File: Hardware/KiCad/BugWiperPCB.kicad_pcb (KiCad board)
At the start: 2 copper layers, 112 x 40 mm, 95 parts, among them J1 UJ20-C-H-G-SMT-1-P16-TR, J2 TBLH10-350-06BK, J3 Phoenix_1776508, J4 RJ45, Q1 NMOS_SO-8, U1 ESP32-S3-WROOM-1, U2 BTN9960LV, U3 BTN9960LV, U4 INA180A2, U5 WE-TVS-82400102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

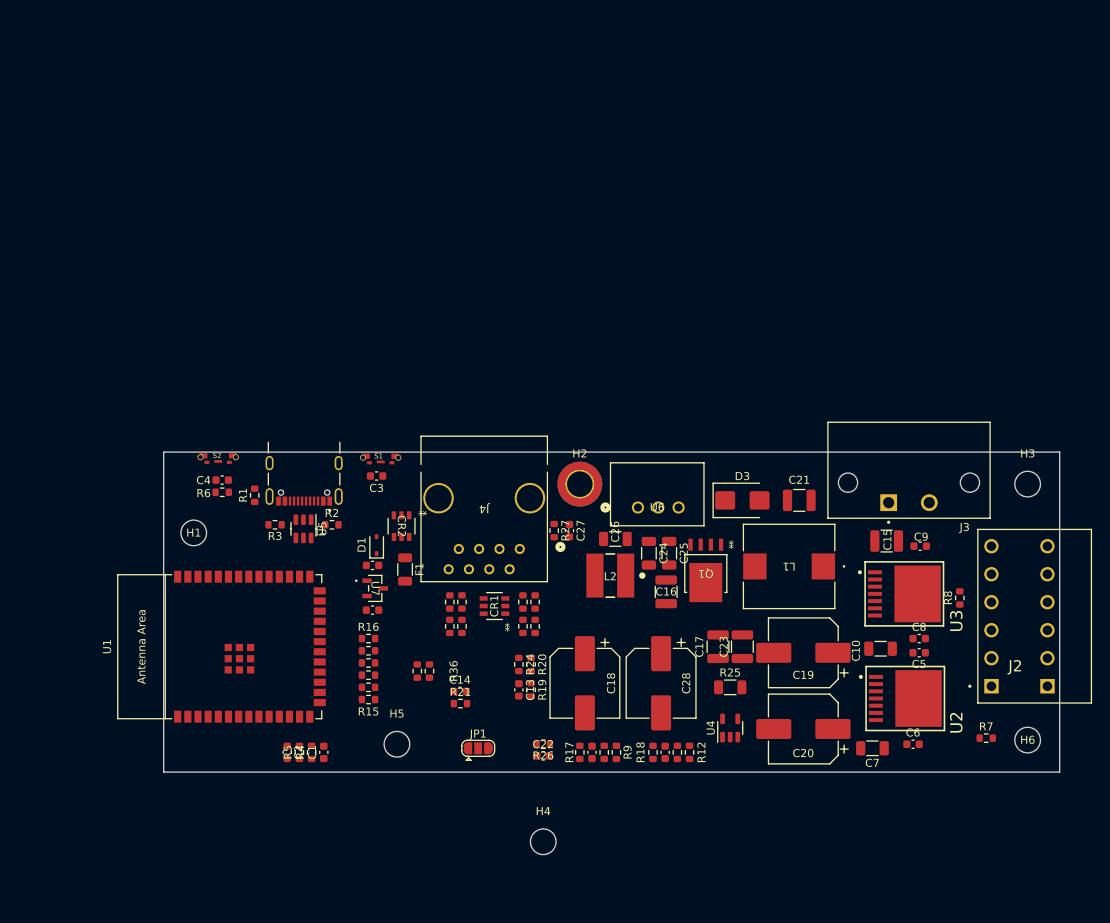
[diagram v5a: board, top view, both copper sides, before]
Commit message: add debug connector, arrange foodprints and add NTC and connect to GPIOs to ESP32
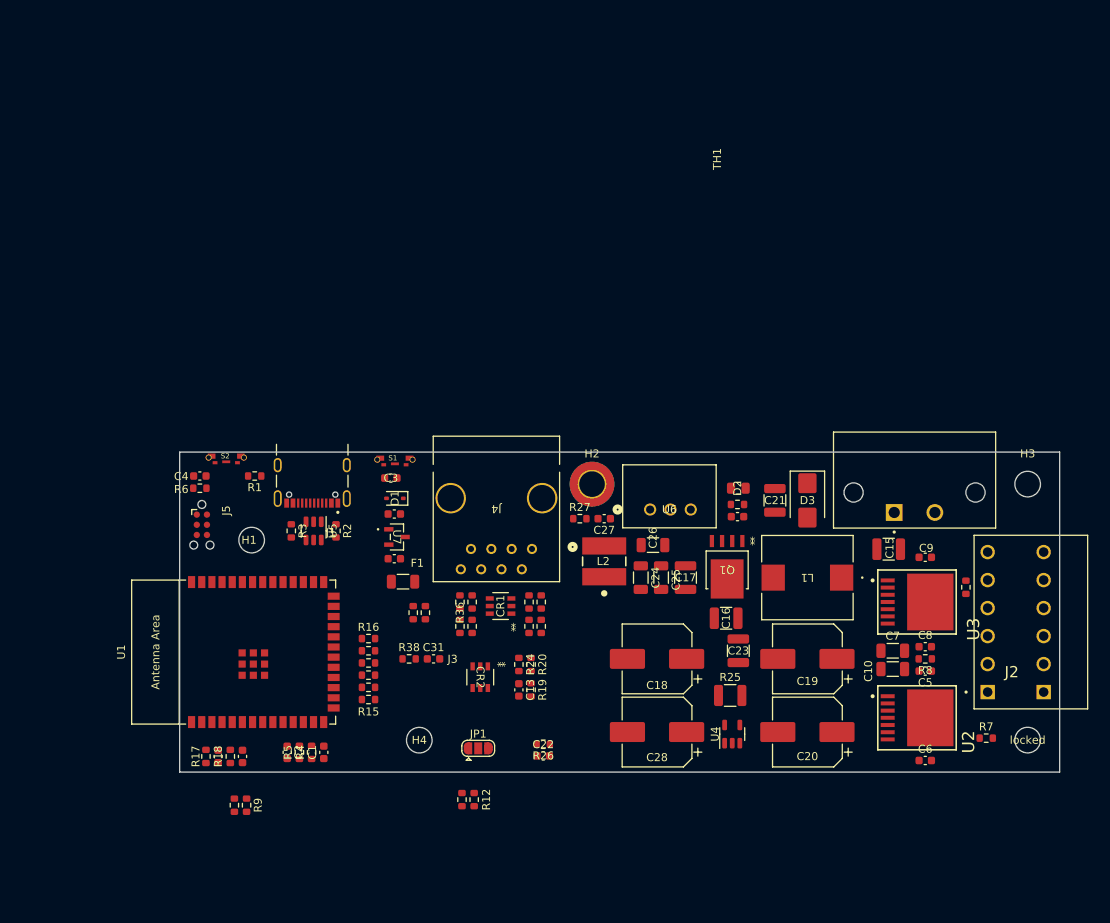
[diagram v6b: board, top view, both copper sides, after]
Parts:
- removed H5: MountingHole, MountingHole:MountingHole_3.2mm_M3_DIN965
- added C31: 100nF, Capacitor_SMD:C_0603_1608Metric, F.Cu at (141.7, 85.9)
- added D2: D_Zener, Resistor_SMD:R_0805_2012Metric, F.Cu at (179.8, 64.5)
- added J5: Conn_TagConnect_TC2030-NL_ESP_Prog, Connector:Tag-Connect_TC2030-IDC-NL_2x03_P1.27mm_Vertical, F.Cu at (112.8, 69.1)
- added R38: 10k, Resistor_SMD:R_0603_1608Metric, F.Cu at (138.7, 85.9)
- added TH1: Thermistor_NTC, Resistor_SMD:R_0603_1608Metric, F.Cu at (208.3, 76.9)
- C4: value 100nF -> 1uF
- R12, R9: value 2k -> 1k
- R25: footprint Resistor_SMD:R_1206_3216Metric -> Resistor_SMD:R_1210_3225Metric
- moved C12 52.8 mm to (117.9, 98.0)
- moved R18 52.8 mm to (116.3, 98.0)
- moved C11 46.7 mm to (114.8, 98.0)
- moved R17 46.7 mm to (113.3, 98.0)
- moved R10 46.7 mm to (116.8, 104.1)
- moved R9 46.7 mm to (118.4, 104.1)
- moved R21 42.6 mm to (179.7, 66.5)
- moved C14 41.0 mm to (179.7, 68.1)
- moved R11 27.6 mm to (145.3, 103.4)
- moved R12 27.6 mm to (146.8, 103.4)
- moved CR2 21.3 mm to (147.6, 88.1)
- moved H4 20.0 mm to (140.0, 96.0)
- moved C7 12.5 mm to (199.1, 84.8), turned to 0 degrees
- moved C17 9.54 mm to (173.2, 75.7)
- moved C18 9.52 mm to (169.7, 85.9), turned to 180 degrees
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- renumbered H6 to locked
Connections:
- net CHIP_PU renamed EN
- net GPIO0 renamed Boot
- C1 pad 2: D+ -> Net-(C1-Pad2)
- C2 pad 1: D- -> Net-(C2-Pad1)
- C22 pad 1: /Power/adc_ina -> /ESP32-S3/ADC_INA
- R17 pad 1: /Power/M_IS1 -> /ESP32-S3/M_IS1
- R18 pad 1: /Power/M_IS2 -> /ESP32-S3/M_IS2
- R24 pad 1: unconnected-(R24-Pad1) -> Net-(U1-GPIO4/TOUCH4/ADC1_CH3)
- R26 pad 2: /Power/adc_ina -> /ESP32-S3/ADC_INA
- R32 pad 1: IN_3 -> IN_4
- R34 pad 1: IN_4 -> IN_3
- R4 pad 1: Net-(U1-GPIO20/U1CTS/ADC2_CH9/CLK_OUT1/USB_D+) -> Net-(C1-Pad2)
- R5 pad 1: Net-(U1-GPIO19/U1RTS/ADC2_CH8/CLK_OUT2/USB_D-) -> Net-(C2-Pad1)
- U1 pad 12: unconnected-(U1-GPIO8/TOUCH8/ADC1_CH7/SUBSPICS1-Pad12) -> OUT1
- U1 pad 13: Net-(U1-GPIO19/U1RTS/ADC2_CH8/CLK_OUT2/USB_D-) -> D-
- U1 pad 14: Net-(U1-GPIO20/U1CTS/ADC2_CH9/CLK_OUT1/USB_D+) -> D+
- U1 pad 17: unconnected-(U1-GPIO9/TOUCH9/ADC1_CH8/FSPIHD/SUBSPIHD-Pad17) -> OUT2
- U1 pad 20: unconnected-(U1-GPIO12/TOUCH12/ADC2_CH1/FSPICLK/FSPIIO6/SUBSPICLK-Pad20) -> IN_1
- U1 pad 21: unconnected-(U1-GPIO13/TOUCH13/ADC2_CH2/FSPIQ/FSPIIO7/SUBSPIQ-Pad21) -> IN_2
- U1 pad 22: unconnected-(U1-GPIO14/TOUCH14/ADC2_CH3/FSPIWP/FSPIDQS/SUBSPIWP-Pad22) -> IN_3
- U1 pad 23: unconnected-(U1-GPIO21-Pad23) -> IN_4
- U1 pad 36: unconnected-(U1-U0RXD/GPIO44/CLK_OUT2-Pad36) -> RX
- U1 pad 37: unconnected-(U1-U0TXD/GPIO43/CLK_OUT1-Pad37) -> TX
- U1 pad 39: unconnected-(U1-GPIO1/TOUCH1/ADC1_CH0-Pad39) -> /ESP32-S3/ADC_NTC
- U1 pad 4: unconnected-(U1-GPIO4/TOUCH4/ADC1_CH3-Pad4) -> Net-(U1-GPIO4/TOUCH4/ADC1_CH3)
- U1 pad 5: unconnected-(U1-GPIO5/TOUCH5/ADC1_CH4-Pad5) -> /ESP32-S3/M_IS1
- U1 pad 6: unconnected-(U1-GPIO6/TOUCH6/ADC1_CH5-Pad6) -> /ESP32-S3/M_IS2
- U1 pad 7: unconnected-(U1-GPIO7/TOUCH7/ADC1_CH6-Pad7) -> /ESP32-S3/ADC_INA
- U5 pad 4: D+ -> Net-(C1-Pad2)
- U5 pad 6: D- -> Net-(C2-Pad1)
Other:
- board size 112 x 40 mm -> 110 x 40 mm

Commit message: add resistor arrays
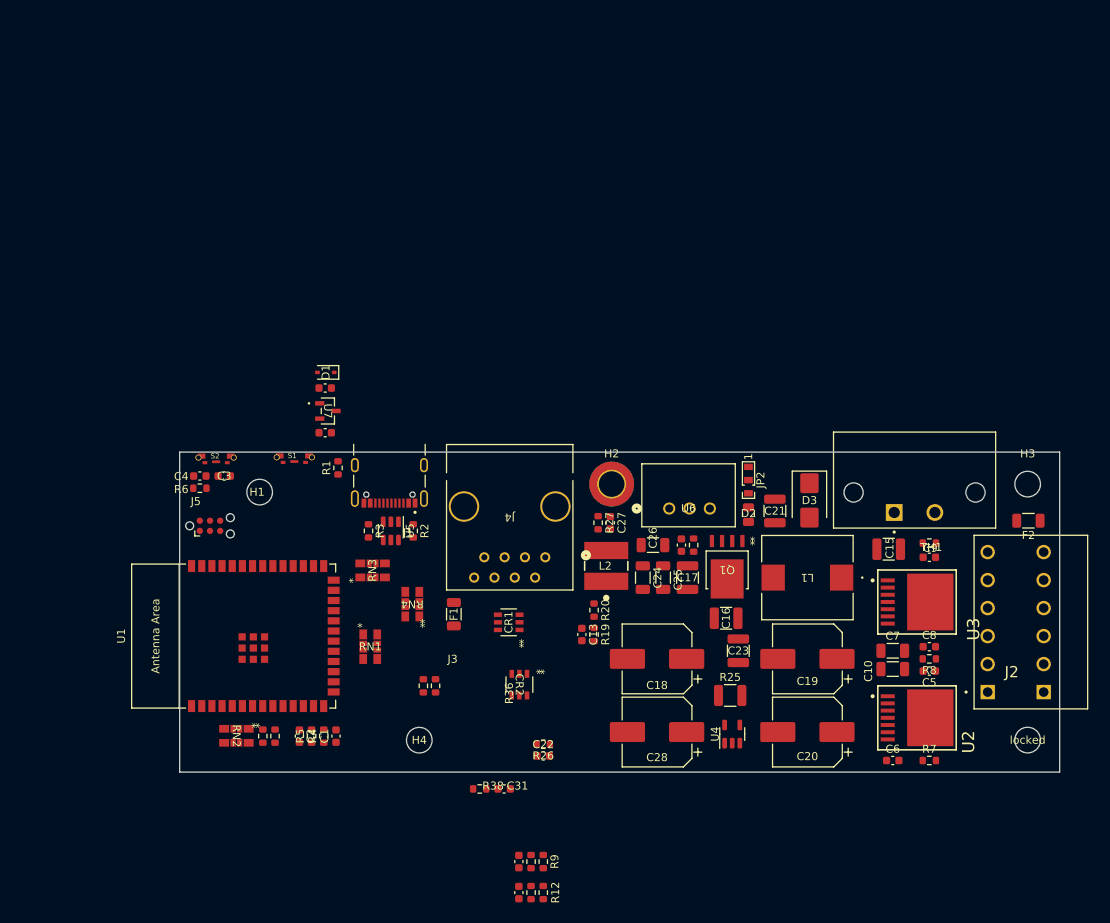
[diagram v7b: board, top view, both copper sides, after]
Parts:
- removed JP1: SolderJumper_3_Bridged12, Jumper:SolderJumper-3_P1.3mm_Open_RoundedPad1.0x1.5mm
- removed R13, R14, R15, R16, R17, R18, R24, R29, R34: 1k, Resistor_SMD:R_0603_1608Metric
- removed R28, R32: 4k7, Resistor_SMD:R_0603_1608Metric
- removed R30, R31, R33, R35: 5k, Resistor_SMD:R_0603_1608Metric
- added F2: 10mA Polyfuse, Resistor_SMD:R_1206_3216Metric, F.Cu at (216.1, 68.6)
- added JP2: SolderJumper_3_Open, BugWiper_lib:SolderJumper_R_SMD_0603, F.Cu at (181.1, 63.5)
- added RN1: 1k_Pack04, BugWiper_lib:BO_CAY16, F.Cu at (133.8, 84.3)
- added RN2: 1k_Pack04, BugWiper_lib:BO_CAY16, F.Cu at (117.1, 95.5)
- added RN3: 10k_Pack04, BugWiper_lib:BO_CAY16, F.Cu at (134.1, 74.8)
- added RN4: 10k_Pack04, BugWiper_lib:BO_CAY16, F.Cu at (139.1, 79.0)
- moved C11 39.8 mm to (152.4, 111.2)
- moved C12 38.5 mm to (152.4, 115.1)
- moved R10 37.7 mm to (153.9, 111.2)
- moved R9 37.7 mm to (155.4, 111.2)
- moved C3 20.8 mm to (115.6, 63.0), turned to 180 degrees
- moved C31 18.5 mm to (150.6, 102.1)
- moved R38 18.5 mm to (147.5, 102.1)
- moved C29 18.0 mm to (128.2, 57.6)
- moved D1 18.0 mm to (128.3, 50.0)
- moved C30 18.0 mm to (128.2, 52.0)
- moved U7 18.0 mm to (128.5, 54.9)
- moved R22 17.0 mm to (120.4, 95.5), turned to -90 degrees
- moved R23 14.8 mm to (121.9, 95.5), turned to -90 degrees
- moved R11 14.5 mm to (153.9, 115.1)
- moved R12 14.5 mm to (155.4, 115.1)
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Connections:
- net +3V3 renamed Net-(J2-3)
- C11 pad 1: Net-(C11-Pad1) -> /ESP32-S3/M_IS1
- C12 pad 1: Net-(C12-Pad1) -> /ESP32-S3/M_IS2
- J4 pad 2: Net-(CR1-IO_2) -> Net-(CR1-IO_1)
- J4 pad 3: Net-(CR1-IO_1) -> Net-(CR1-IO_2)
- J4 pad 6: Net-(CR1-IO_4) -> Net-(CR1-IO_3)
- J4 pad 7: Net-(CR1-IO_3) -> Net-(CR1-IO_4)
- R10 pad 1: Net-(C11-Pad1) -> /ESP32-S3/M_IS1
- R11 pad 1: Net-(C12-Pad1) -> /ESP32-S3/M_IS2
- U1 pad 18: unconnected-(U1-GPIO10/TOUCH10/ADC1_CH9/FSPICS0/FSPIIO4/SUBSPICS0-Pad18) -> M__IN1
- U1 pad 19: unconnected-(U1-GPIO11/TOUCH11/ADC2_CH0/FSPID/FSPIIO5/SUBSPID-Pad19) -> M__IN2
- U1 pad 20: IN_1 -> M__INH1
- U1 pad 21: IN_2 -> M__INH2
- U1 pad 22: IN_3 -> IN_1
- U1 pad 23: IN_4 -> IN_2
- U1 pad 24: unconnected-(U1-GPIO47/SPICLK_P/SUBSPICLK_P_DIFF-Pad24) -> IN_3
- U1 pad 25: unconnected-(U1-GPIO48/SPICLK_N/SUBSPICLK_N_DIFF-Pad25) -> IN_4
- U1 pad 39: /ESP32-S3/ADC_NTC -> A_INA
- U1 pad 4: Net-(U1-GPIO4/TOUCH4/ADC1_CH3) -> A_VBAT
- U1 pad 5: /ESP32-S3/M_IS1 -> A_NTC
- U1 pad 6: /ESP32-S3/M_IS2 -> A_IS2
- U1 pad 7: /ESP32-S3/ADC_INA -> A_IS1
- U1 pad 8: unconnected-(U1-GPIO15/U0RTS/ADC2_CH4/XTAL_32K_P-Pad8) -> Enc1
- U1 pad 9: unconnected-(U1-GPIO16/U0CTS/ADC2_CH5/XTAL_32K_N-Pad9) -> Enc2
- U2 pad 3: Net-(U2-IN) -> /ESP32-S3/M_IN1
- U2 pad 4: Net-(U2-INH) -> /ESP32-S3/M_INH1
- U3 pad 3: Net-(U3-IN) -> /ESP32-S3/M_IN2
- U3 pad 4: Net-(U3-INH) -> /ESP32-S3/M_IHN2

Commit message: begin routing
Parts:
- removed R22, R23, R26: 1k, Resistor_SMD:R_0603_1608Metric
- removed R36, R37: 330, Resistor_SMD:R_0603_1608Metric
- added R13: 1k, Resistor_SMD:R_0603_1608Metric, F.Cu at (149.3, 92.5)
- added RN5: 1k_Pack04, BugWiper_lib:BO_CAY16, F.Cu at (121.9, 95.0)
- added RN6: 100R_Pack04, BugWiper_lib:BO_CAY16, F.Cu at (148.8, 80.8)
- added RN7: 100R_Pack04, BugWiper_lib:BO_CAY16, F.Cu at (154.4, 80.8)
- D1: footprint Diode_SMD:D_SOD-323 -> Diode_SMD:D_SOD-323_HandSoldering
- RN3: value 10k_Pack04 -> 47k_Pack04
- RN4: value 10k_Pack04 -> 2k2_Pack04
- moved C2 28.3 mm to (138.9, 70.9), turned to 90 degrees
- moved C1 25.0 mm to (133.9, 70.9), turned to -90 degrees
- moved C11 20.8 mm to (154.4, 90.5)
- moved C12 20.8 mm to (154.4, 94.4)
- moved R10 20.8 mm to (156.0, 90.5)
- moved R11 20.8 mm to (156.0, 94.4)
- moved R12 20.8 mm to (157.5, 94.4)
- moved R9 20.8 mm to (157.5, 90.5)
- moved D1 15.8 mm to (129.5, 65.8), turned to 90 degrees
- moved C30 12.9 mm to (126.2, 64.8)
- moved U7 12.6 mm to (126.5, 67.3)
- moved C29 12.4 mm to (126.2, 69.8)
- moved C22 9.36 mm to (149.3, 90.9)
- moved R38 5.19 mm to (148.6, 97.0), turned to -90 degrees
- moved C31 5.10 mm to (150.1, 97.0), turned to 90 degrees
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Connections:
- net Net-(D3-A2) renamed /Power/+VBat*
- C22 pad 1: /ESP32-S3/ADC_INA -> A_INA
- CR2 pad 4: EN_C1 -> Net-(CR2-IO_3)
- CR2 pad 6: EN_C2 -> Net-(CR2-IO_4)
- J4 pad 2: Net-(CR1-IO_1) -> Net-(RN7C-R3.1)
- J4 pad 3: Net-(CR1-IO_2) -> Net-(RN7D-R4.1)
- J4 pad 4: OUT_1 -> Net-(RN6-R1.1)
- J4 pad 5: OUT_2 -> Net-(RN6-R2.1)
- J4 pad 6: Net-(CR1-IO_3) -> Net-(RN6-R3.1)
- J4 pad 7: Net-(CR1-IO_4) -> Net-(RN6-R4.1)
- RN4 pad 1: Net-(CR1-IO_1) -> Net-(CR1-IO_4)
- RN4 pad 2: Net-(CR1-IO_2) -> Net-(CR1-IO_3)
- RN4 pad 3: Net-(CR1-IO_3) -> Net-(CR1-IO_1)
- RN4 pad 4: Net-(CR1-IO_4) -> Net-(CR1-IO_2)
- U4 pad 1: Net-(R26-Pad1) -> /ESP32-S3/ADC_INA
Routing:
- net +12V_HighSide: track 0.00 -> 5.43 mm
- added copper zone on F.Cu, net +12V_HighSide
- added copper zone on F.Cu, net /Power/+VBat
- added copper zone on F.Cu, net /Power/+VBat*
- added copper zone on F.Cu, net GND
- added copper zone on F.Cu, net Motor+
- added copper zone on F.Cu, net Motor-
